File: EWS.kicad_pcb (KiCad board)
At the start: 4 copper layers, 65 x 56 mm, 122 parts, among them J301 GPIO, J401 XT30, J402 MX3.0 2x2, J403 MX3.0 2x2, J404 USB-C, J405 USB-C, J406 USB-A, Q401 CJAC70P06, Q402 CJAC70P06, Q403 AO3400A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

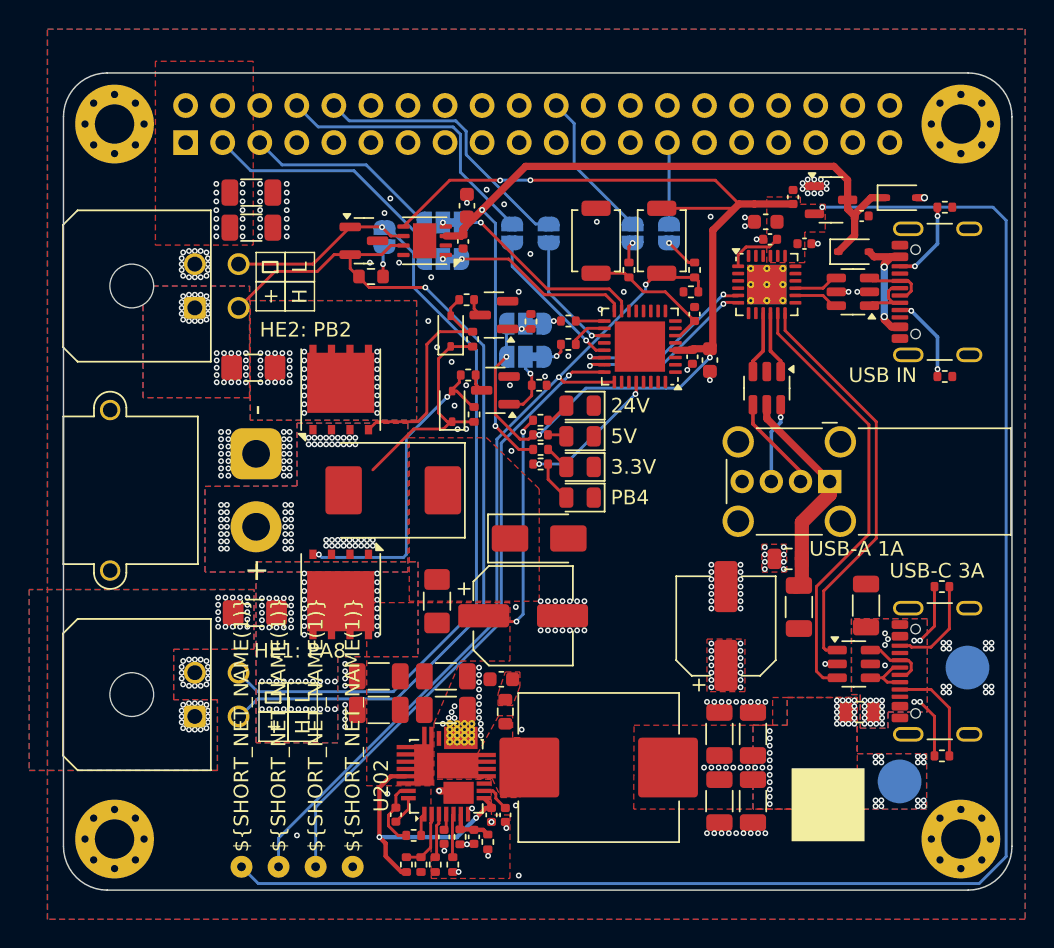
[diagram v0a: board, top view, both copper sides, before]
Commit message: docs: Update unreleased changes in changelog and README
- Fixed USB hub controller (U401/CH334): XO pin connected to GND for crystal-less operation
- Fixed DC/DC converter (U202/XR76208): Enable circuit changed to Zener diode for 12V operation
- Fixed USB outputs: Replaced fuses with TPS2557 power distribution switches for backfeed protection
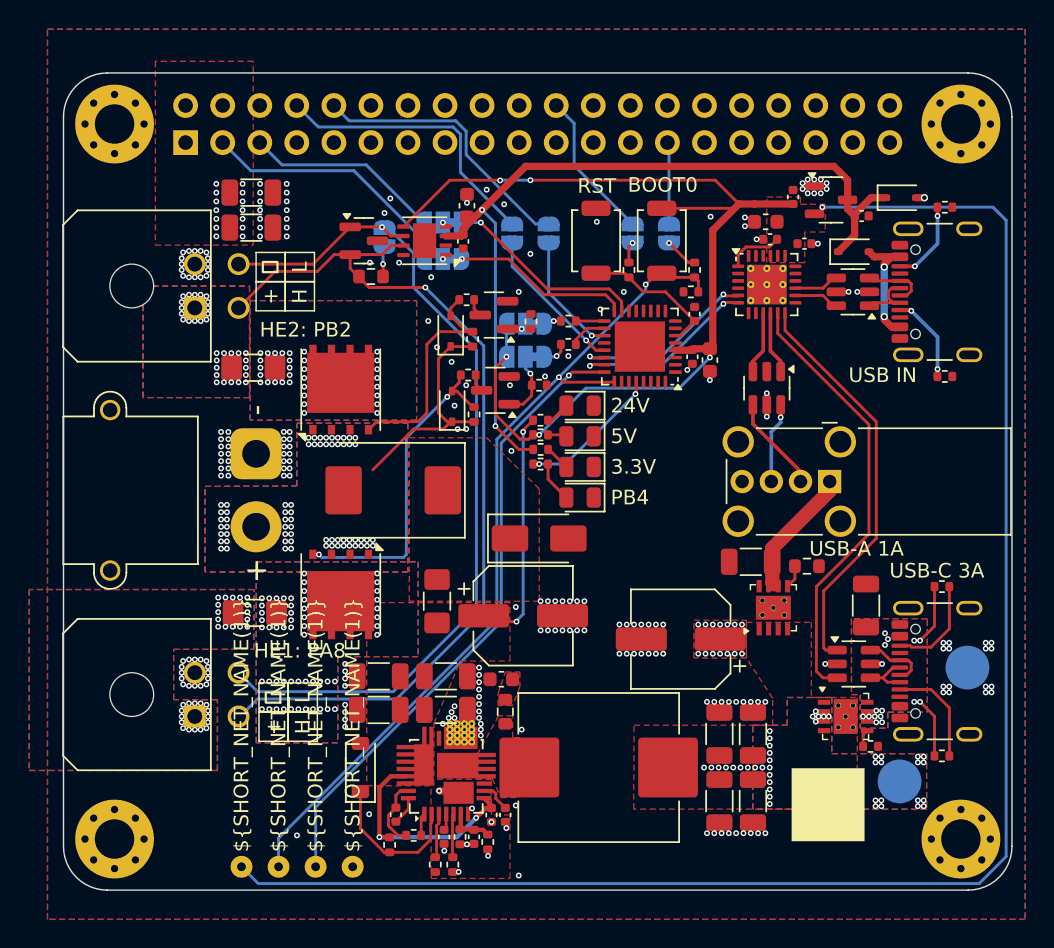
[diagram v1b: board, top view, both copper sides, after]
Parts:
- removed F403: 4A, Fuse:Fuse_0805_2012Metric
- removed F404: 1.5A, Fuse:Fuse_0805_2012Metric
- removed R205: 2k2, Resistor_SMD:R_0402_1005Metric
- added D204: BZT52C4V7, Diode_SMD:D_SOD-123, F.Cu at (150.3, 114.6)
- added R413: 33k, Resistor_SMD:R_0402_1005Metric, F.Cu at (185.3, 113.2)
- added R414: 68k, Resistor_SMD:R_0603_1608Metric, F.Cu at (180.9, 100.8)
- added U405: TPS2557, project:S-PVSON-N8, F.Cu at (183.6, 111.1)
- added U406: TPS2557, project:S-PVSON-N8, F.Cu at (178.7, 103.7)
- R204: value 100k -> 10k
- moved C406 4.53 mm to (177.1, 100.5), turned to 180 degrees
- moved C403 3.23 mm to (172.3, 105.8), turned to 180 degrees
- moved R204 1.77 mm to (152.3, 119.9)
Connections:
- C405 pad 1: Net-(U403-VBUS) -> /Connectivity/5VC
- C406 pad 1: Net-(J406-VBUS) -> /Connectivity/5VA
- J405 pad A4: Net-(U403-VBUS) -> /Connectivity/5VC
- J405 pad A9: Net-(U403-VBUS) -> /Connectivity/5VC
- J405 pad B4: Net-(U403-VBUS) -> /Connectivity/5VC
- J405 pad B9: Net-(U403-VBUS) -> /Connectivity/5VC
- J406 pad 1: Net-(J406-VBUS) -> /Connectivity/5VA
- R204 pad 1: /Power/VIN -> /Power/EN
- R204 pad 2: /Power/EN -> /Power/VIN
- R411 pad 2: Net-(U403-VBUS) -> /Connectivity/5VC
- R412 pad 2: Net-(U403-VBUS) -> /Connectivity/5VC
- U401 pad 4: unconnected-(U401-XI-Pad4) -> GND
- U403 pad 5: Net-(U403-VBUS) -> 5V
- U404 pad 5: Net-(J406-VBUS) -> 5V
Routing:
- net Net-(J406-VBUS): track 15.2 -> 0.00 mm
- net /Connectivity/5VA: track 0.00 -> 8.73 mm
- net Net-(U403-VBUS): track 8.22 -> 0.00 mm, vias 22 -> 0
- net /Connectivity/5VC: track 0.00 -> 8.22 mm, vias 0 -> 15
- net /Power/EN: track 4.25 -> 10.2 mm
- net /Power/VIN: track 34.9 -> 32.3 mm
- net 5V: track 2.75 -> 5.15 mm, vias 90 -> 77
- net Net-(U406-I_{LIM}): track 0.00 -> 1.58 mm
- net Net-(U405-I_{LIM}): track 0.00 -> 1.19 mm
- added copper zone on B.Cu, net /Connectivity/5VC
- added copper zone on F.Cu, net /Connectivity/5VC
- removed copper zone on B.Cu, net Net-(U403-VBUS)
- removed copper zone on F.Cu, net Net-(U403-VBUS)
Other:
- board text added: "RST"
